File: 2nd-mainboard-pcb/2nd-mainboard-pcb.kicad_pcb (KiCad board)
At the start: 4 copper layers, 99 x 97.5 mm, 131 parts, among them J1 PJ-082BH, J10 Servo Motor BL Touch, J11 T3, J12 Steckverbinder_Male_Fans, J13 Steckverbinder_Female_Leistung, J14 FAN3, J15 Steckverbinder_Female_Motoren, J16 ISP, J18 Quartz, J19 T2, J2 Fan_12/5V_Regelung, J20 T2, J21 T2, J22 T3, J23 Conn_01x04_Socket, J24 Steckverbinder_Male_Leistung, J3 Fan_12/5V_Regelung, J4 FAN0, J5 FAN1, J6 FAN2, J7 Stepper Motor, J8 Servo Motor SM, J9 Microstepping, P1 USB_C_Receptacle_USB2.0_14P, SW3 PTS820 J25K SMTR LFS, U1 SQJ409EP-T1_GE3, U10 ATmega328PB-A, U12 MPU-6050, U2 SZ1SMB5927BT3G, U3 TPS56837HRPAR, U4 TPS565208, U5 FT232RL, U7 TPM16050-S6TR, U8 RJK0456DPB-00-J5, U9 RJK0456DPB-00-J5, Y1 ECS-160-18-4X-CKM

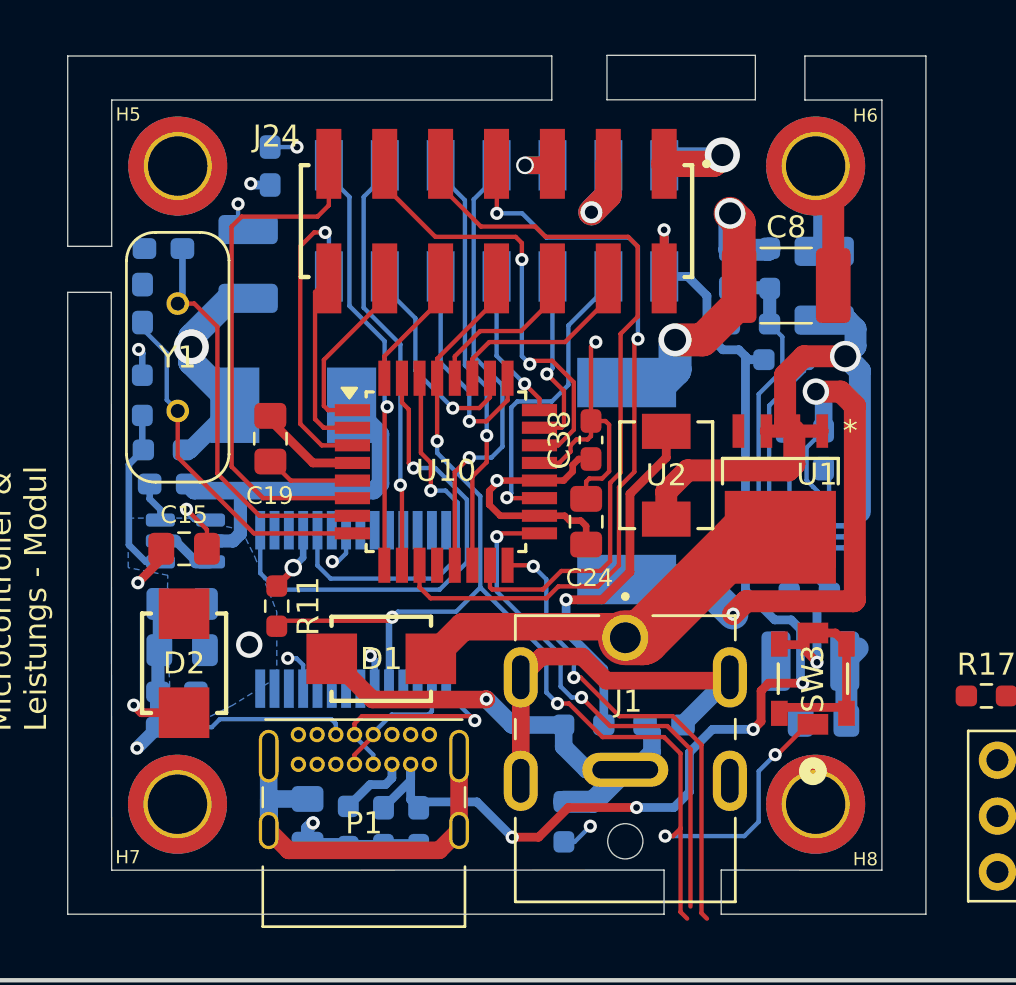
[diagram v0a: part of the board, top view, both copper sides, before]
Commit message: made better connections
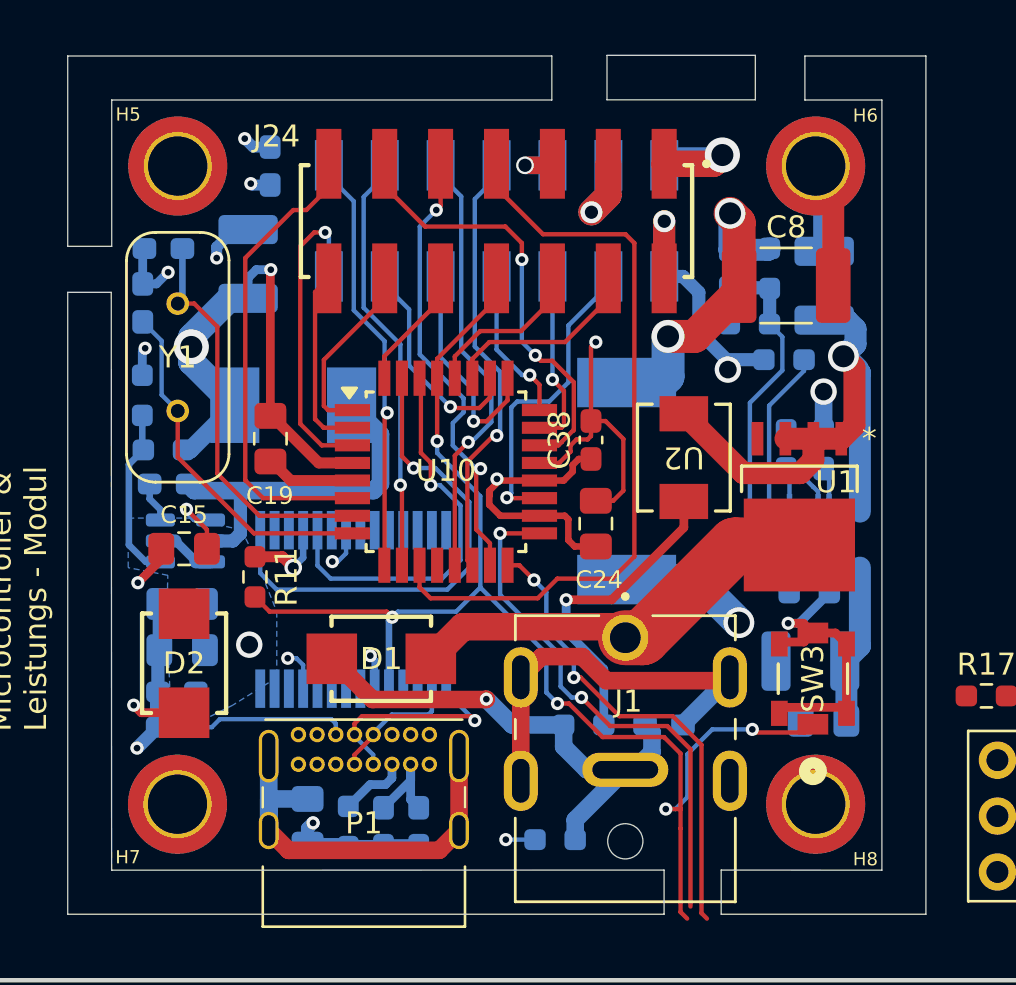
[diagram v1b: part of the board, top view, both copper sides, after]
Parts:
- moved R11 1.66 mm to (109.0, 131.7)
- moved U2 1.13 mm to (128.5, 126.2), turned to -90 degrees
- moved U1 0.93 mm to (133.8, 129.0)
- moved R6 0.90 mm to (122.7, 143.6), turned to 180 degrees
- moved C24 0.45 mm to (124.5, 129.2)
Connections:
- U10 pad 13: FAN_01_PWM_clockwise -> FAN_01_PWM_counterclockwise
- U10 pad 14: FAN_01_PWM_counterclockwise -> FAN_01_PWM_clockwise
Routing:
- net AREF: track 81.7 -> 43.8 mm, vias 9 -> 6
- net Net-(U3-SW): track 28.3 -> 12.0 mm
- net MOSI: track 33.0 -> 20.7 mm, vias 0 -> 2
- net +5V_POW: track 22.5 -> 31.9 mm, vias 4 -> 5
- net GND: track 80.0 -> 83.1 mm, vias 12 -> 13
- net Net-(U1-G): track 16.9 -> 14.3 mm
- net LED_MOT0: track 23.7 -> 21.5 mm
- net PWR_IN_PROT: track 32.2 -> 33.5 mm
- net FAN_01_PWM_clockwise: track 20.6 -> 19.9 mm
- net GND2: track 22.3 -> 23.0 mm
- net +24V: track 18.6 -> 19.3 mm
- net STEP: track 35.0 -> 34.4 mm, vias 2 -> 0
- net FAN_01_PWM_counterclockwise: track 19.3 -> 19.9 mm
- net RESET: track 61.1 -> 61.6 mm
- added copper zone on In2.Cu, net Net-(U3-SW)

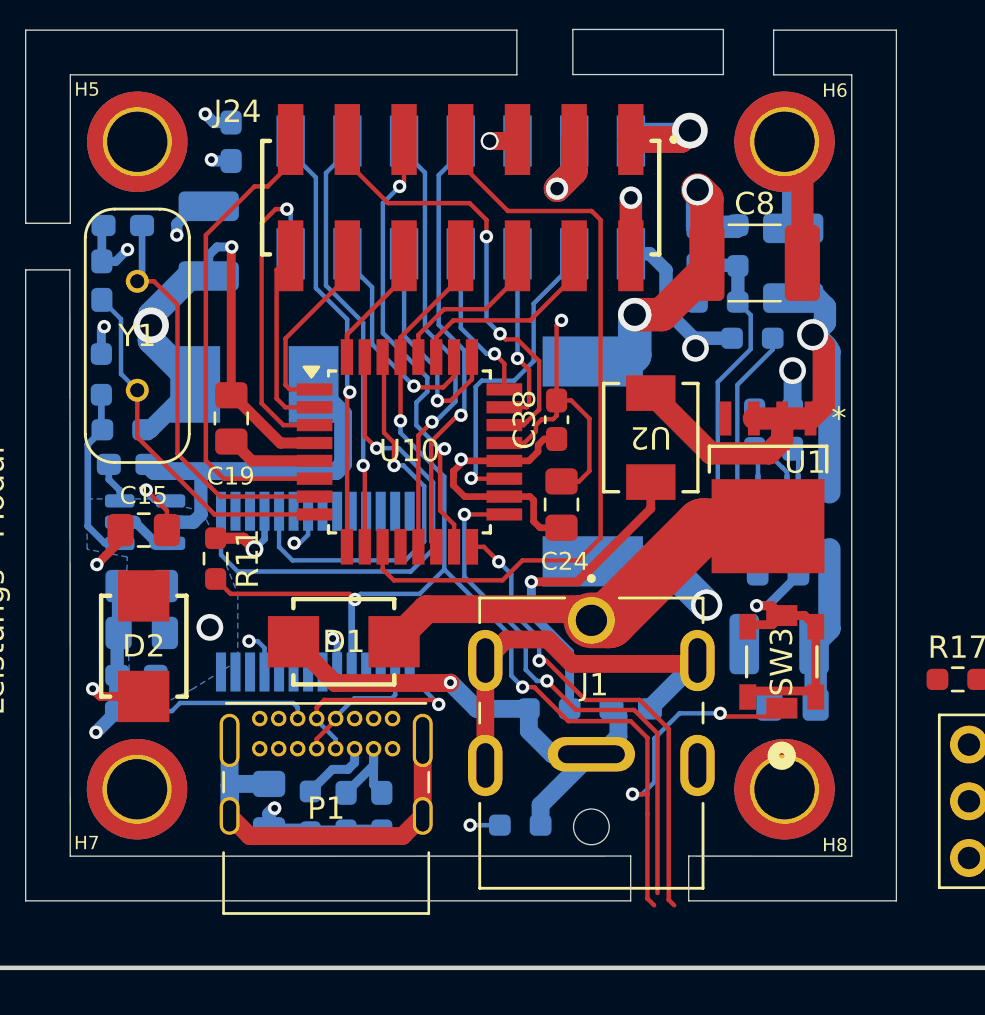
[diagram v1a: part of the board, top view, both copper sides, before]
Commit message: volle zonen auf b.cu erstellt und schaltregler symbol ausgetauscht
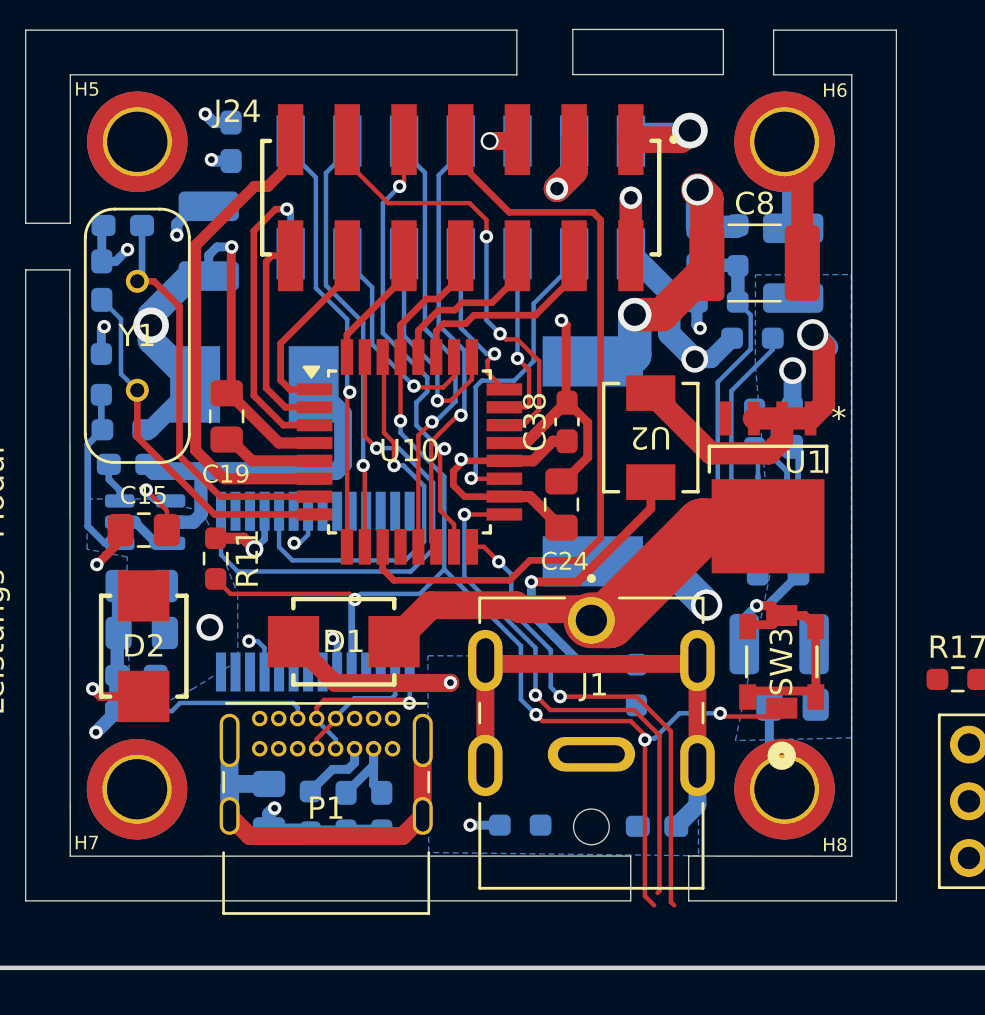
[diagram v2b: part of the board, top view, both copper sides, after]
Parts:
- removed U3: TPS56837HRPAR, Imported_Component_Footprints:TPS56837HRPAR
- added U6: TPS56837RPAR, Imported_Component_Footprints:CONV_TPS56837RPAR, B.Cu at (134.2, 129.6)
- moved C7 5.39 mm to (128.8, 143.7)
- moved R1 4.05 mm to (127.9, 137.3), turned to -90 degrees
- moved C38 0.48 mm to (124.8, 125.5)
- moved C19 0.23 mm to (109.5, 125.3)
- moved C1 0.09 mm to (134.8, 125.8)
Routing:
- net PWR_IN_PROT: track 33.5 -> 15.8 mm
- net GND2: track 23.0 -> 7.80 mm
- net GND: track 83.1 -> 89.2 mm, vias 13 -> 14
- net GND3: track 18.1 -> 22.1 mm
- net RESET: track 61.6 -> 58.9 mm
- net USBD+: track 9.88 -> 7.95 mm
- net BLT_Switch: track 8.52 -> 9.39 mm
- net Net-(U1-G): track 14.3 -> 15.0 mm
- added copper zone on B.Cu, net GND2
- added copper zone on B.Cu, net PWR_IN_PROT

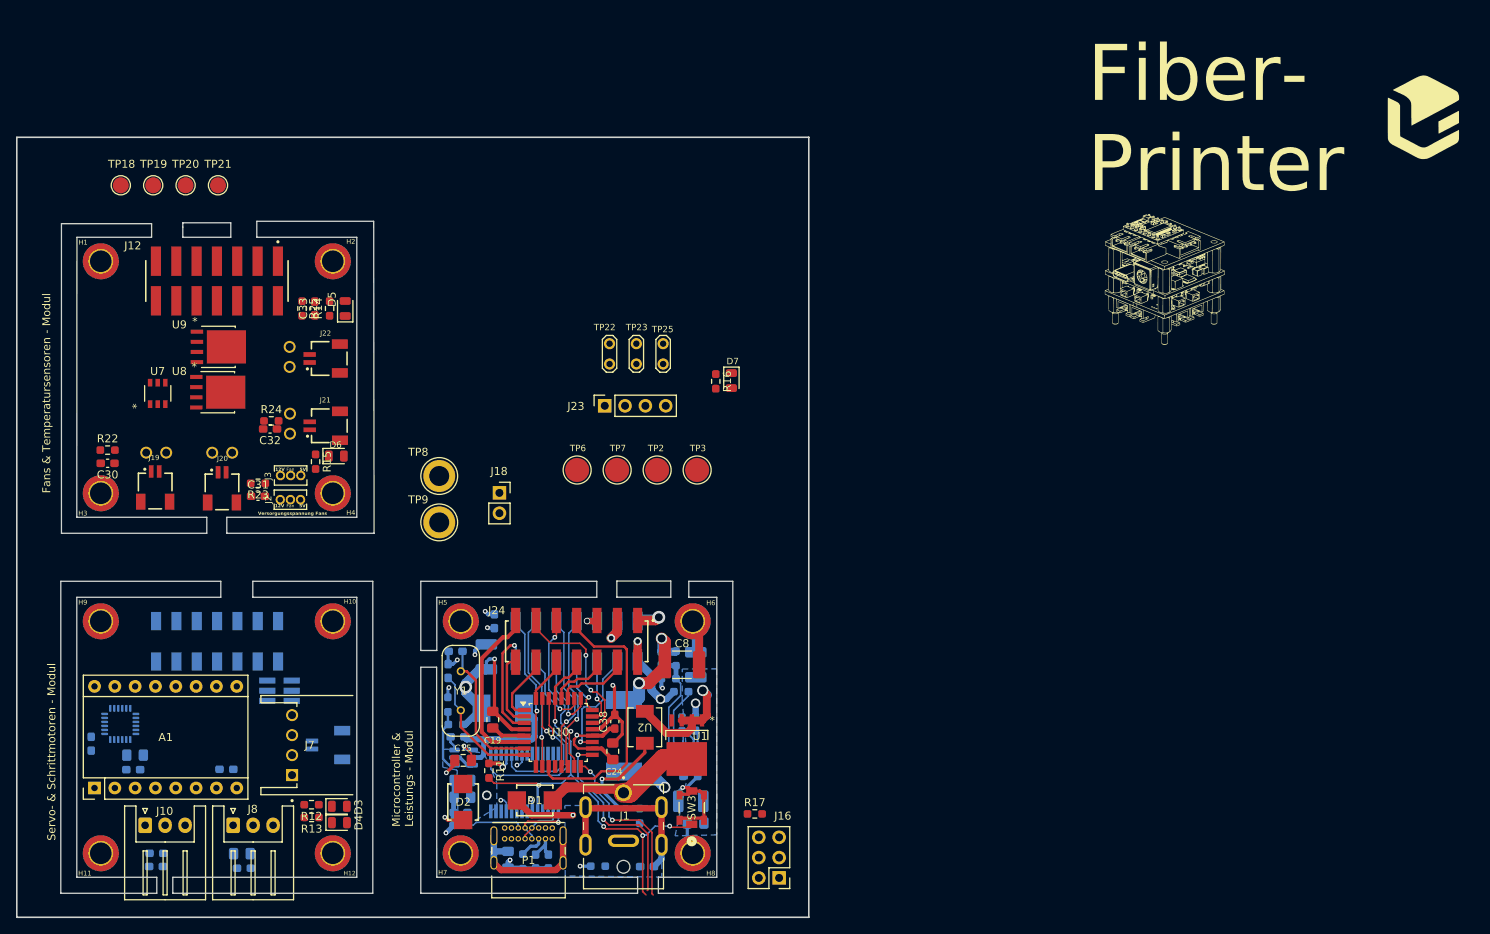
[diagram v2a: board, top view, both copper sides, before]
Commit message: Made traces thicker
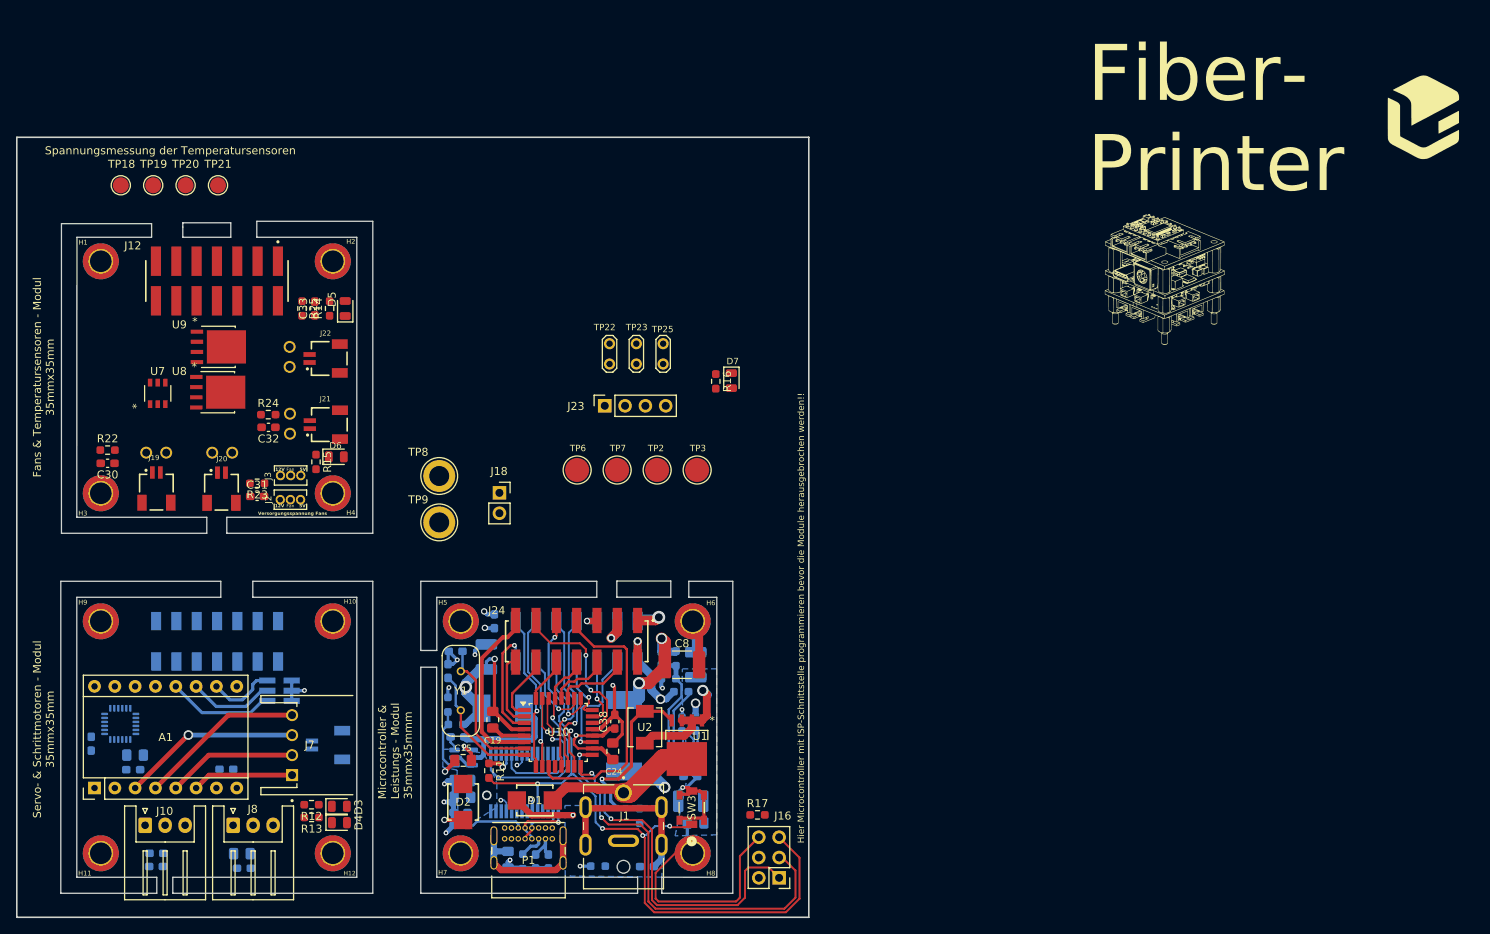
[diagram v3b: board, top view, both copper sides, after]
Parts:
- moved R24 0.87 mm to (81.4, 87.2)
- moved R17 0.36 mm to (142.6, 137.2)
- moved C32 0.28 mm to (81.5, 88.8)
- moved J19 0.20 mm to (67.5, 96.3)
- moved J21 0.14 mm to (88.5, 88.4)
- moved C31 0.11 mm to (80.0, 97.4)
- moved R23 0.10 mm to (80.0, 95.8)
- moved D6 0.09 mm to (89.9, 92.4)
- moved J20 0.08 mm to (75.6, 96.3)
- moved C36 0.07 mm to (76.3, 79.9)
- moved R15 0.06 mm to (87.4, 93.1)
- turned U2 to 90 degrees
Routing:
- net GND: track 89.2 -> 124.2 mm, vias 14 -> 17
- net RESET: track 58.9 -> 89.9 mm
- net SCK: track 24.6 -> 51.3 mm
- net STP_A2: track 0.00 -> 22.4 mm, vias 0 -> 1
- net MISO: track 22.1 -> 44.2 mm
- net STP_A1: track 0.00 -> 20.8 mm
- net STP_B1: track 0.00 -> 16.2 mm
- net M2: track 0.00 -> 13.4 mm
- net STP_B2: track 0.00 -> 12.7 mm
- net M1: track 0.00 -> 10.8 mm
- net M0: track 0.00 -> 8.42 mm
- net Net-(U1-G): track 15.0 -> 23.1 mm
- net +5V_POW: track 31.9 -> 36.4 mm, vias 5 -> 6
- net RXD: track 18.0 -> 19.0 mm
- net TXD: track 22.6 -> 23.5 mm
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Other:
- outline, holes or cut-outs redrawn
- board text added: "Fans & Temperatursensoren - Modul 35mmx35mm"
- board text added: "Hier Microcontroller mit ISP-Schnittstelle programmieren bevor die Module herausgebrochen werden!!"
- board text added: "Microcontroller & Leistungs - Modul 35mmx35mmm"
- board text added: "Servo- & Schrittmotoren - Modul 35mmx35mm"
- board text added: "Spannungsmessung der Temperatursensoren"
- board text removed: "Fans & Temperatursensoren - Modul"
- board text removed: "Microcontroller & Leistungs - Modul"
- board text removed: "Servo- & Schrittmotoren - Modul"
